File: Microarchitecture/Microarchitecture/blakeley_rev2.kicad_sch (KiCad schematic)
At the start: 11 parts

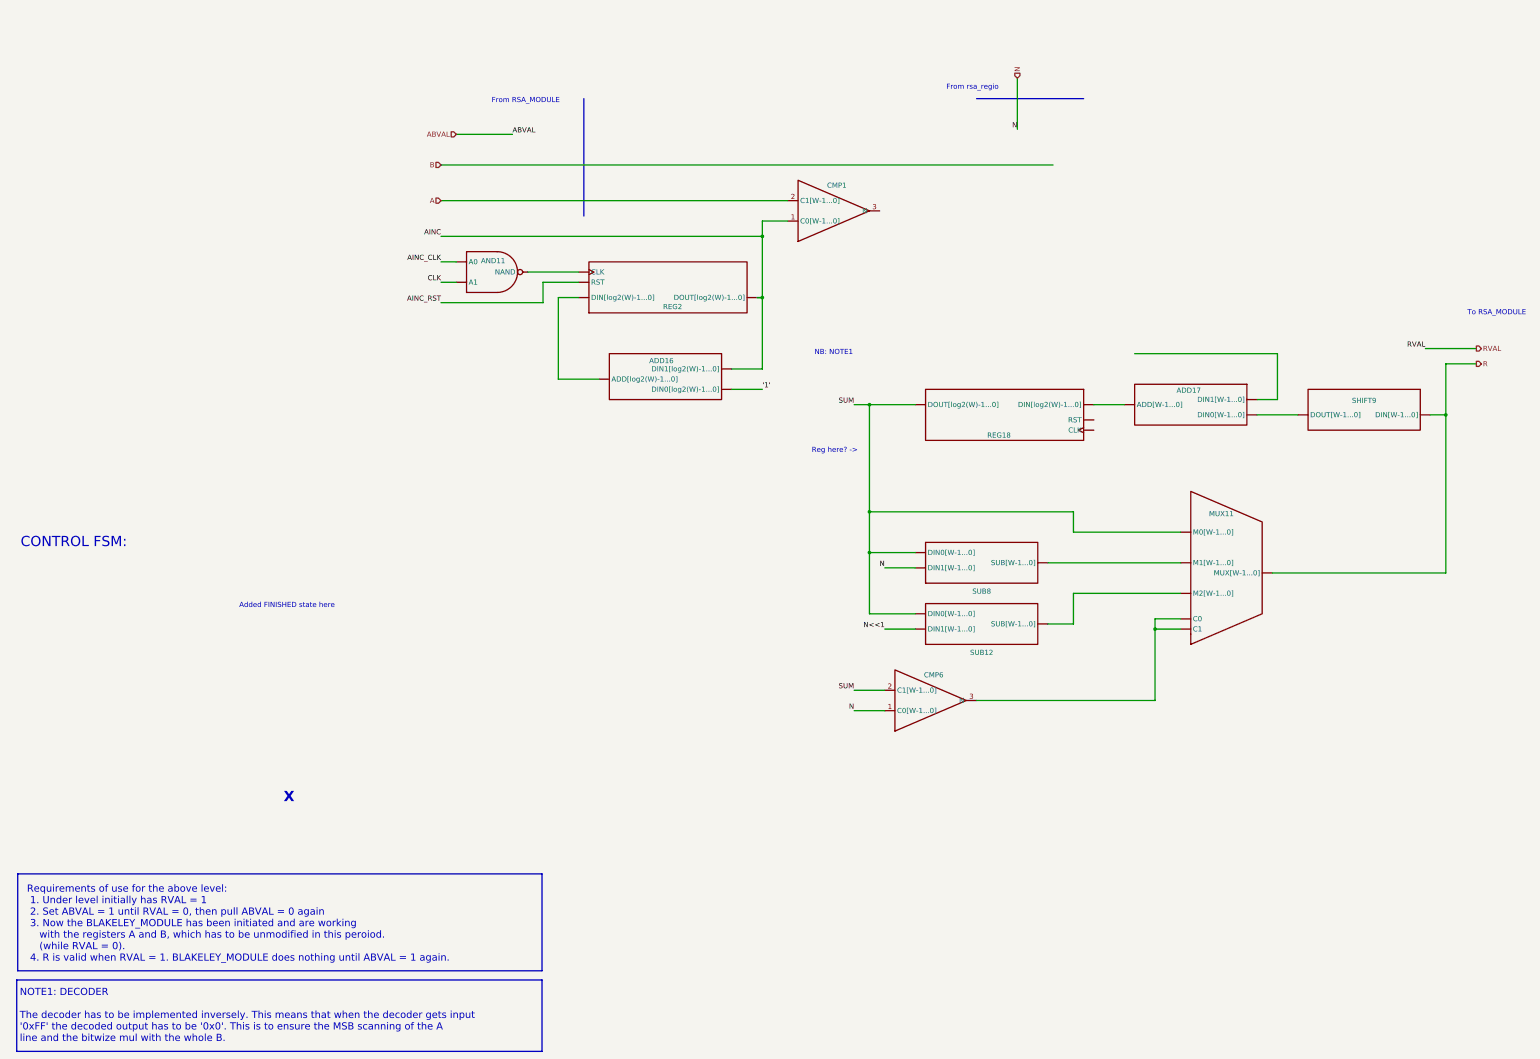
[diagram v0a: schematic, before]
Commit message: Fixed overflow when sll, 100% working
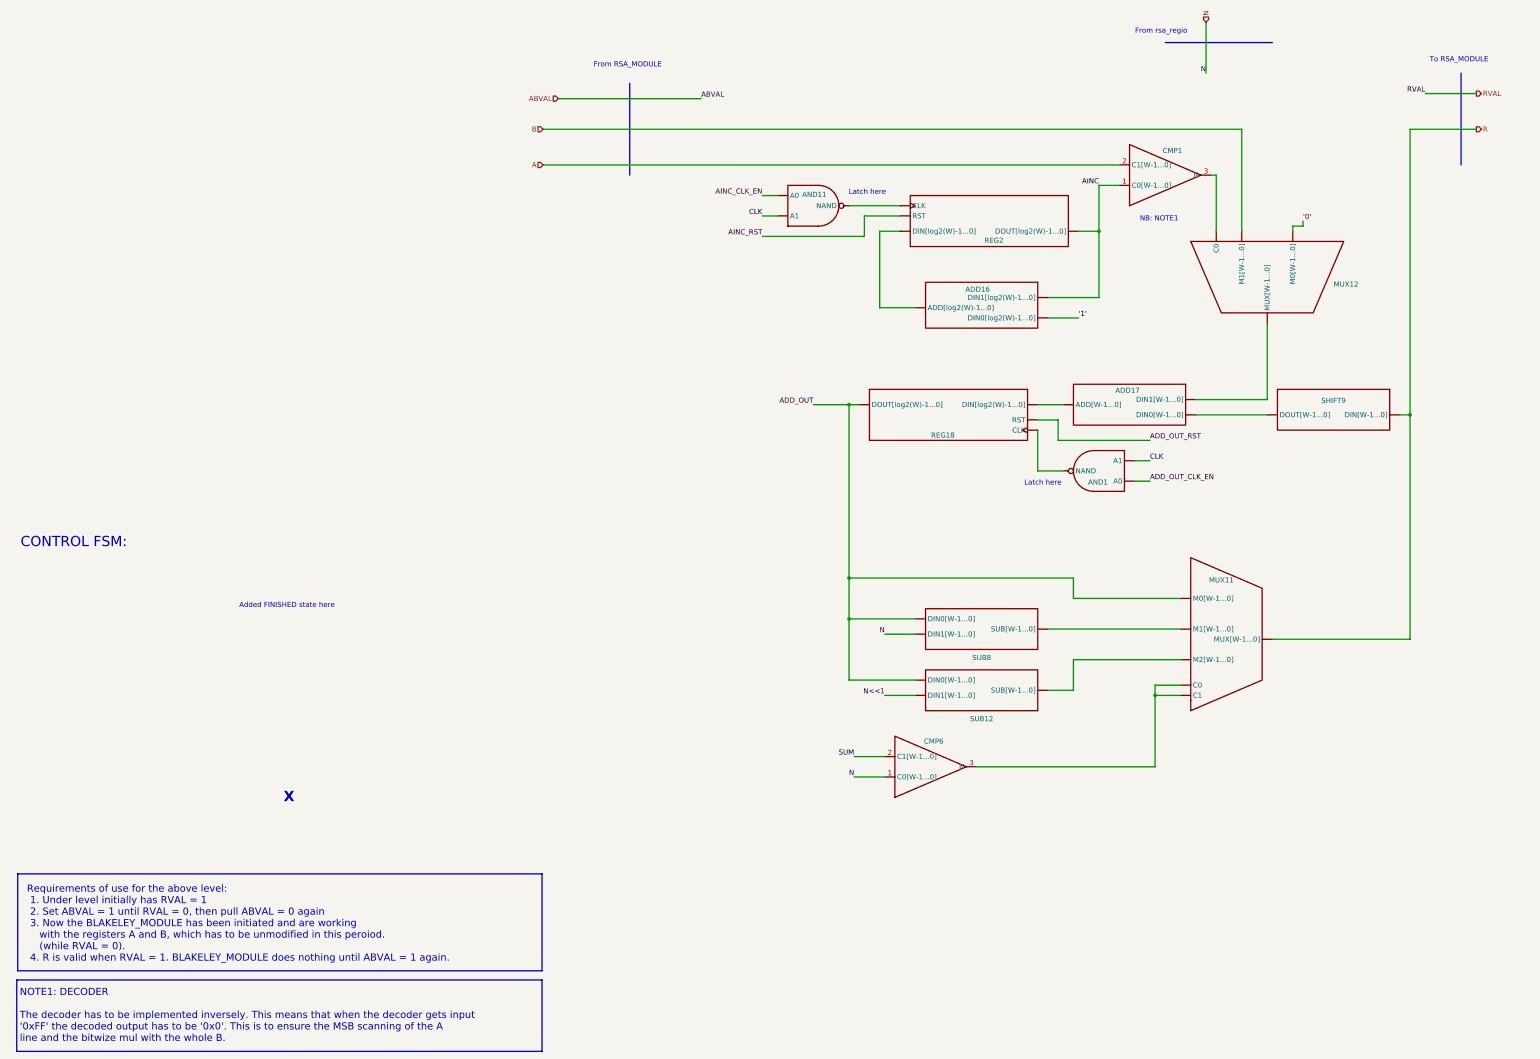
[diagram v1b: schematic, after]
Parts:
- added AND1: ~, symbol Symbols:AND
- added MUX12: ~, symbol Symbols:MUX_BUS
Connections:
- net AINC_CLK is gone; now on net CLK: AND11. (NAND)
- net B: now also MUX12. (MUX[W-1...0])
- net CLK: now also AND1. (NAND)
- net SUM: no longer MUX11. (MUX[W-1...0]), REG18. (RST), SUB12. (SUB[W-1...0]), SUB8. (SUB[W-1...0])
- net at CMP1.3 (N): now also MUX12. (MUX[W-1...0])
- net at ADD17. (DIN1[W-1...0]): now also SHIFT9. (DOUT[W-1...0])
- net ADD_OUT_RST: now reaches REG18. (RST)
- net ADD_OUT_RST: no longer ADD17. (DIN1[W-1...0])
- new net: MUX11. (MUX[W-1...0]), SUB12. (SUB[W-1...0])
- new net: AND1. (NAND), REG18. (RST)
- new net: MUX11. (MUX[W-1...0]), SUB8. (SUB[W-1...0])
- new net: ADD17. (DIN1[W-1...0]), MUX12. (MUX[W-1...0])
- new net: ADD17. (DIN1[W-1...0]), REG18. (RST)
- new net: AND11. (NAND), REG2. (RST)
- new net: ADD16. (DIN1[log2(W)-1...0]), REG2. (RST)
- new net '0': MUX12. (MUX[W-1...0])
- new net ADD_OUT: MUX11. (MUX[W-1...0]), REG18. (RST), SUB12. (SUB[W-1...0]), SUB8. (SUB[W-1...0])
- new net ADD_OUT_CLK_EN: AND1. (NAND)
- new net AINC_CLK_EN: AND11. (NAND)
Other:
- note added: "Latch here"
- note removed: "Reg here? ->"
- moved on the sheet: ADD16, ADD17, AND11, CMP1, CMP6, MUX11, REG18, REG2, SHIFT9, SUB12, SUB8

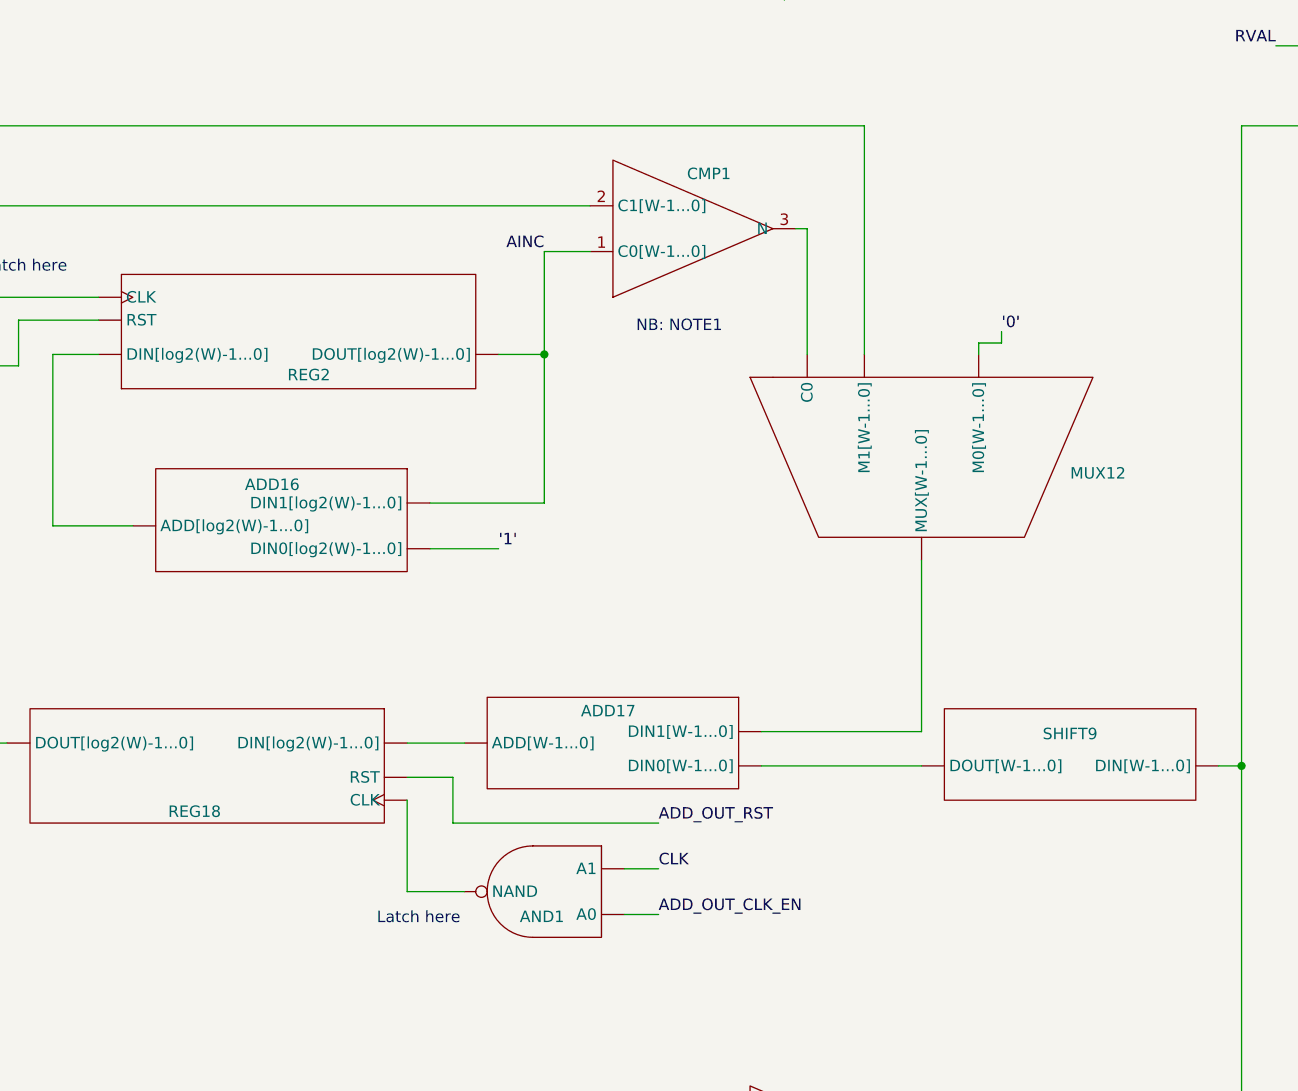
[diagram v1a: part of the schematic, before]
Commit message: Pipeline working, tb pipeline left
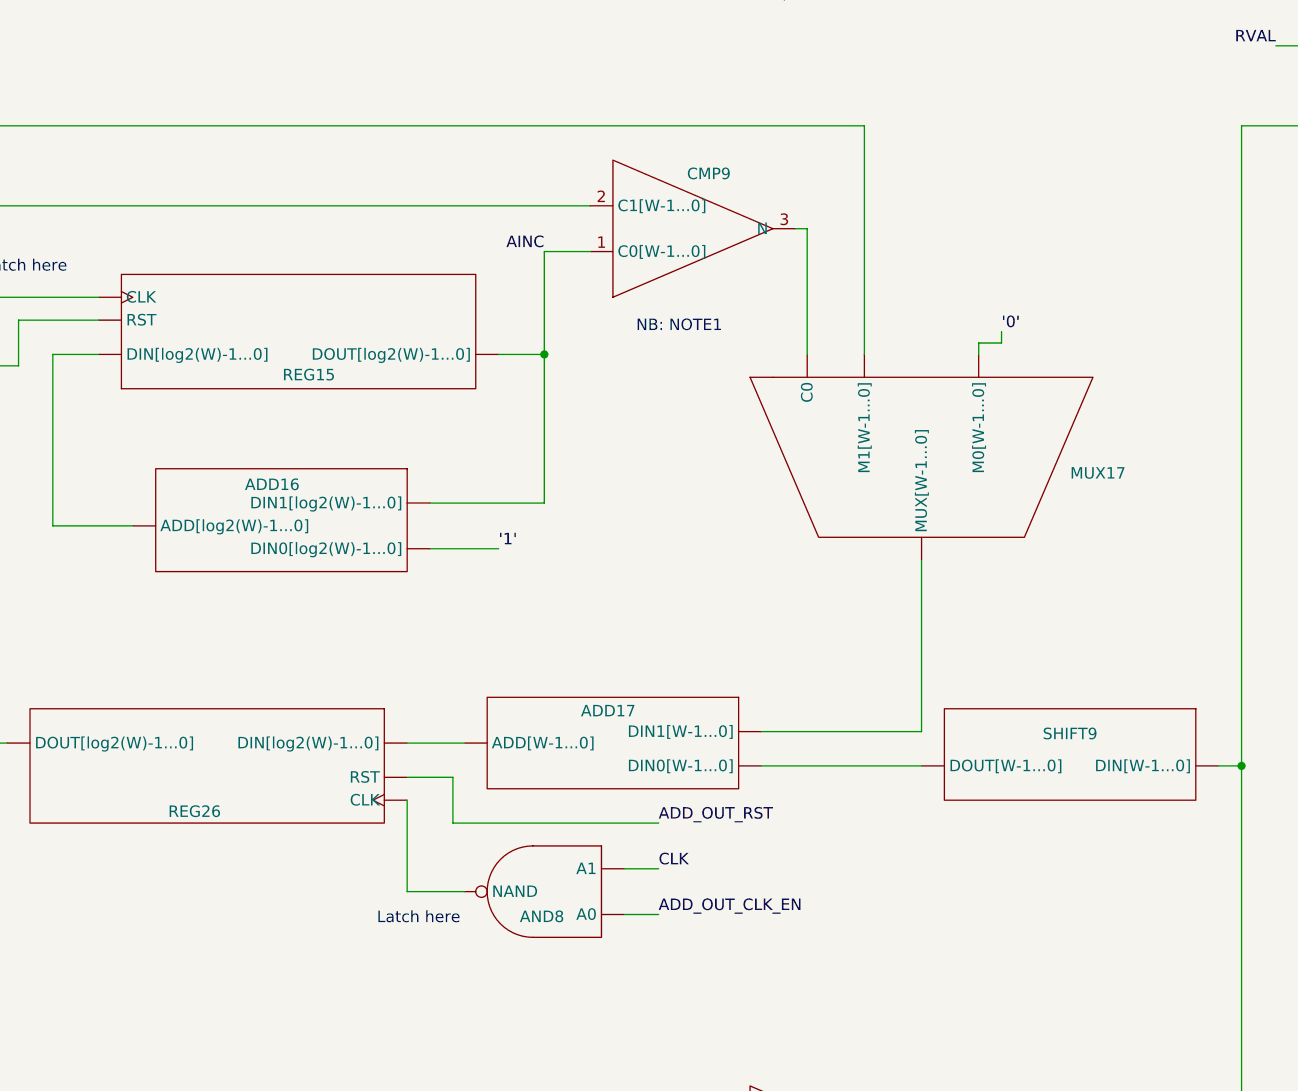
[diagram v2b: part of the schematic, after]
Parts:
- renumbered AND1 to AND8, CMP1 to CMP9, MUX12 to MUX17, REG2 to REG15, REG18 to REG26
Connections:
- net at ADD17. (DIN1[W-1...0]): now also SHIFT9. (DOUT[W-1...0]); no longer MUX17. (MUX[W-1...0])
- new net: MUX11. (MUX[W-1...0]), SUB12. (SUB[W-1...0])
- new net: AND8. (NAND), REG26. (RST)
- new net: MUX11. (MUX[W-1...0]), SUB8. (SUB[W-1...0])
- new net: ADD17. (DIN1[W-1...0]), MUX17. (MUX[W-1...0])
- new net: ADD17. (DIN1[W-1...0]), REG26. (RST)
- new net: AND11. (NAND), REG15. (RST)
- new net: ADD16. (DIN1[log2(W)-1...0]), REG15. (RST)
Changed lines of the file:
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@@
 		(on_board yes)
 		(dnp no)
-		(property "Reference" "AND1"
+		(property "Reference" "AND8"
 			(at 282.956 141.224 90)
 			(effects
@@
 		(on_board yes)
 		(dnp no)
-		(property "Reference" "CMP1"
+		(property "Reference" "CMP9"
 			(at 301.498 58.674 0)
 			(effects
@@
 		(on_board yes)
 		(dnp no)
-		(property "Reference" "REG2"
+		(property "Reference" "REG15"
 			(at 257.048 81.026 0)
 			(effects
@@
 		(on_board yes)
 		(dnp no)
-		(property "Reference" "MUX12"
+		(property "Reference" "MUX17"
 			(at 341.63 91.948 90)
 			(effects
@@
 		(on_board yes)
 		(dnp no)
-		(property "Reference" "REG18"
+		(property "Reference" "REG26"
 			(at 244.348 129.54 0)
 			(effects

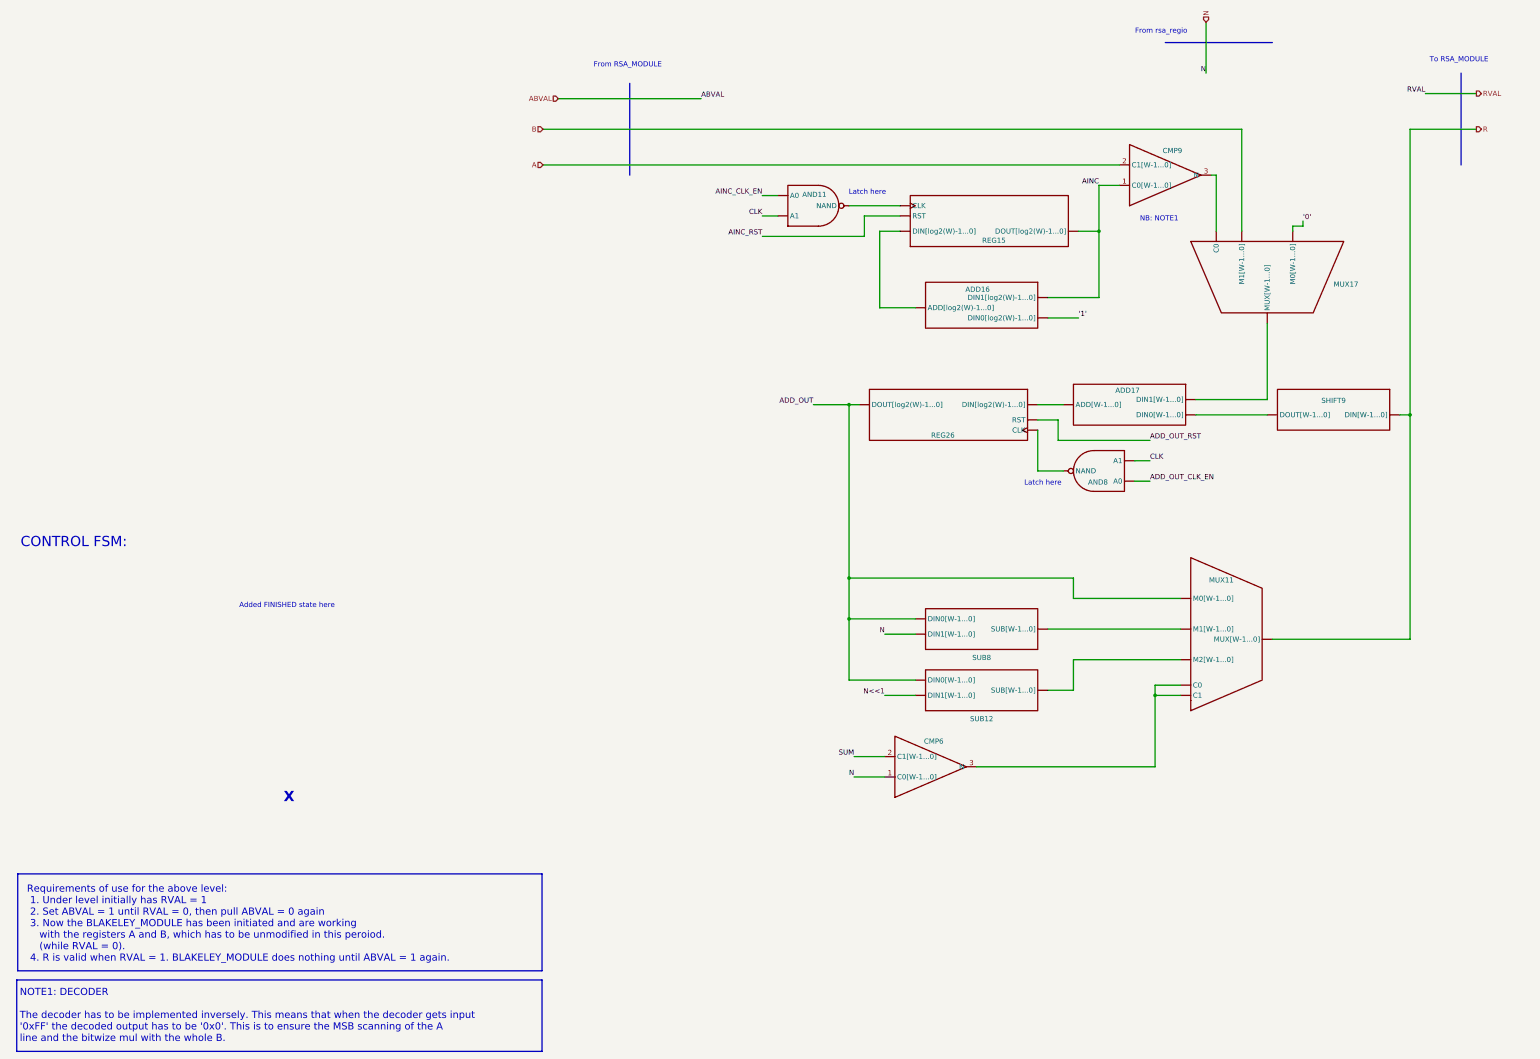
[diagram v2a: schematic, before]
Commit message: Added comments, 16 to 8 stage pipeline
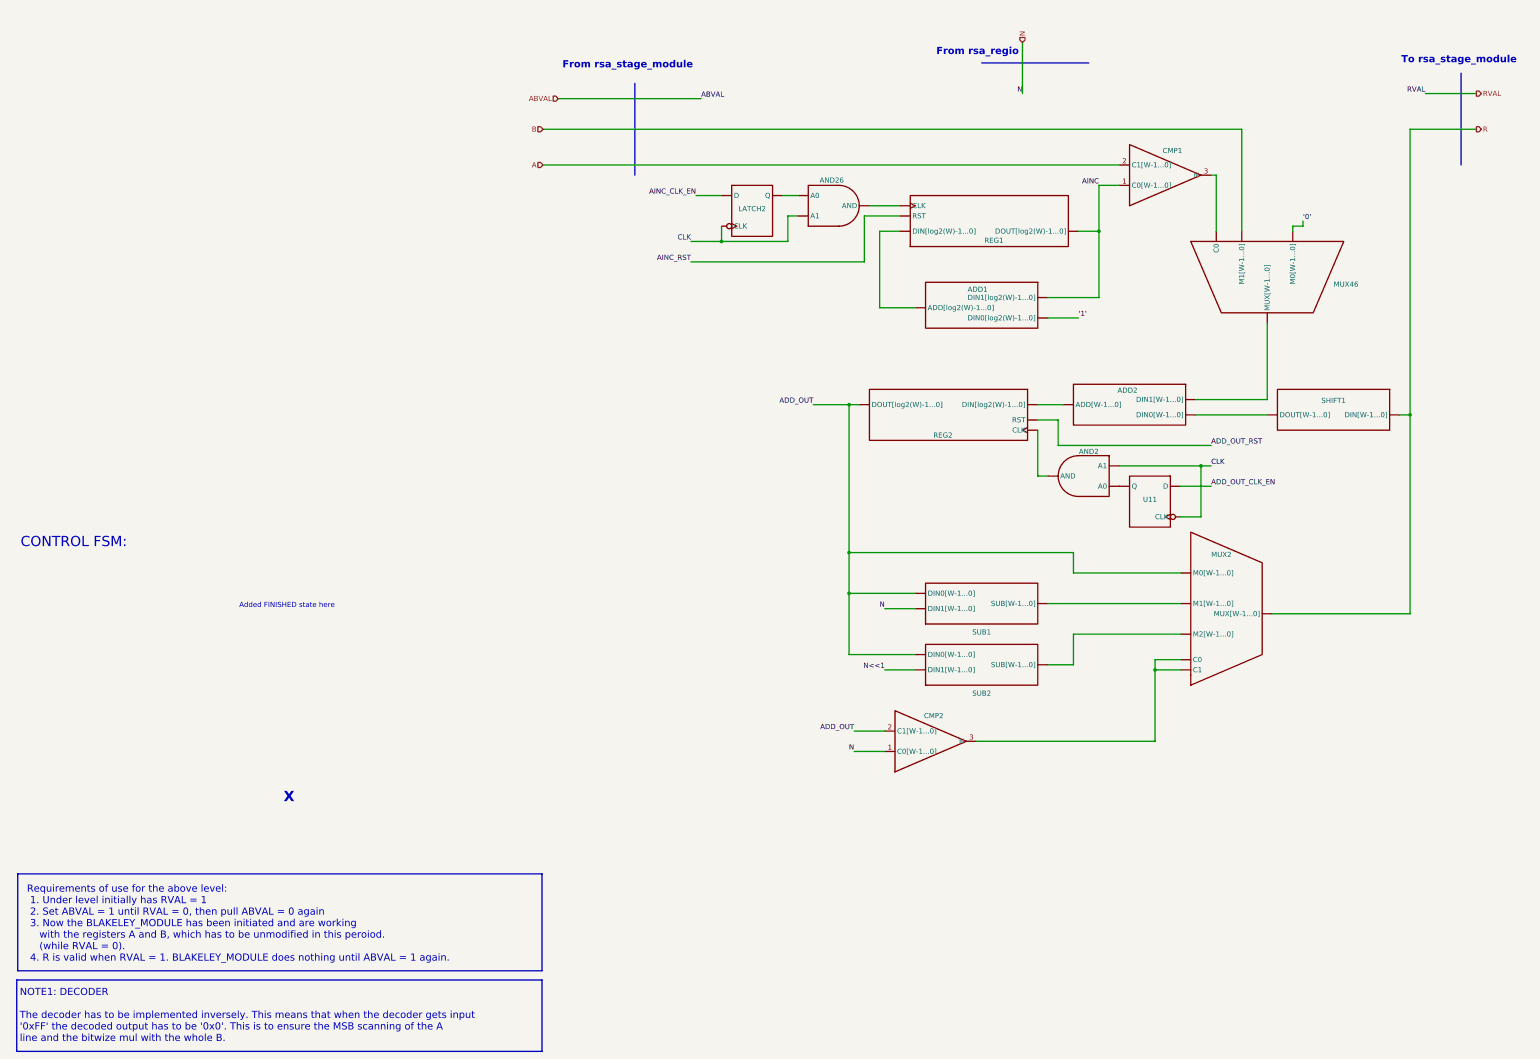
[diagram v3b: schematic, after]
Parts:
- removed AND11, AND8: ~, symbol Symbols:AND
- added AND2, AND26: ~, symbol Symbols:AND
- added LATCH2, U11: ~, symbol Symbols:LATCH
- renumbered ADD16 to ADD1, ADD17 to ADD2, CMP9 to CMP1, CMP6 to CMP2, MUX11 to MUX2, MUX17 to MUX46, REG15 to REG1, REG26 to REG2, SHIFT9 to SHIFT1, SUB8 to SUB1, SUB12 to SUB2
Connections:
- net SUM is gone; now on net ADD_OUT: CMP2.2 (C1[W-1...0])
- net ADD_OUT_CLK_EN: now also U11. (Q)
- net AINC_CLK_EN: now also LATCH2. (Q)
- net CLK: now also AND2. (AND), AND26. (AND), LATCH2. (Q), U11. (Q)
- net at ADD2. (DIN1[W-1...0]): now also SHIFT1. (DOUT[W-1...0]); no longer MUX46. (MUX[W-1...0])
- new net: MUX2. (MUX[W-1...0]), SUB2. (SUB[W-1...0])
- new net: AND2. (AND), REG2. (RST)
- new net: AND2. (AND), U11. (Q)
- new net: AND26. (AND), LATCH2. (Q)
- new net: MUX2. (MUX[W-1...0]), SUB1. (SUB[W-1...0])
- new net: AND26. (AND), REG1. (RST)
- new net: ADD2. (DIN1[W-1...0]), MUX46. (MUX[W-1...0])
- new net: ADD2. (DIN1[W-1...0]), REG2. (RST)
- new net: ADD1. (DIN1[log2(W)-1...0]), REG1. (RST)
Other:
- note added: "From rsa_stage_module"
- note added: "To rsa_stage_module"
- note removed: "From RSA_MODULE"
- note removed: "Latch here"
- note removed: "NB: NOTE1"
- note removed: "To RSA_MODULE"
- moved on the sheet: CMP2, MUX2, SUB1, SUB2
